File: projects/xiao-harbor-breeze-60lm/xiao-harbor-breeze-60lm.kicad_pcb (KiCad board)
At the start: 2 copper layers, 45.8 x 48.3 mm, 43 parts, among them CN1 XY122R-5.08-2P, CN2 XY122R-5.08-2P, J1 1165SDIG-07, J2 1165SDIG-07, Q1 UMW8205A, U1 BQ25185DLHR, U2 ME6210A33PG, U3 DW01A_C351410

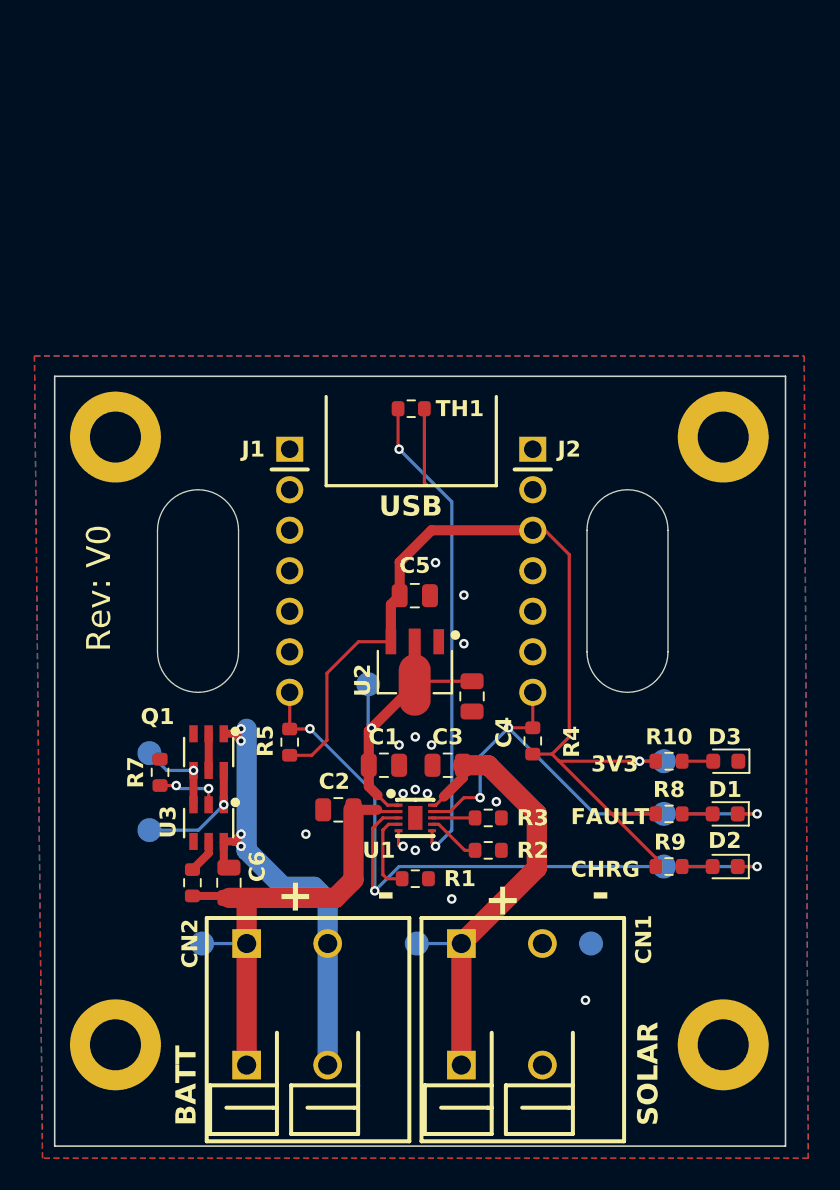
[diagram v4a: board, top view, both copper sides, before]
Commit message: Add user documented LED jumpers
Indicates to users that the LEDs are optional and documents how and
where to cut to conserve power.
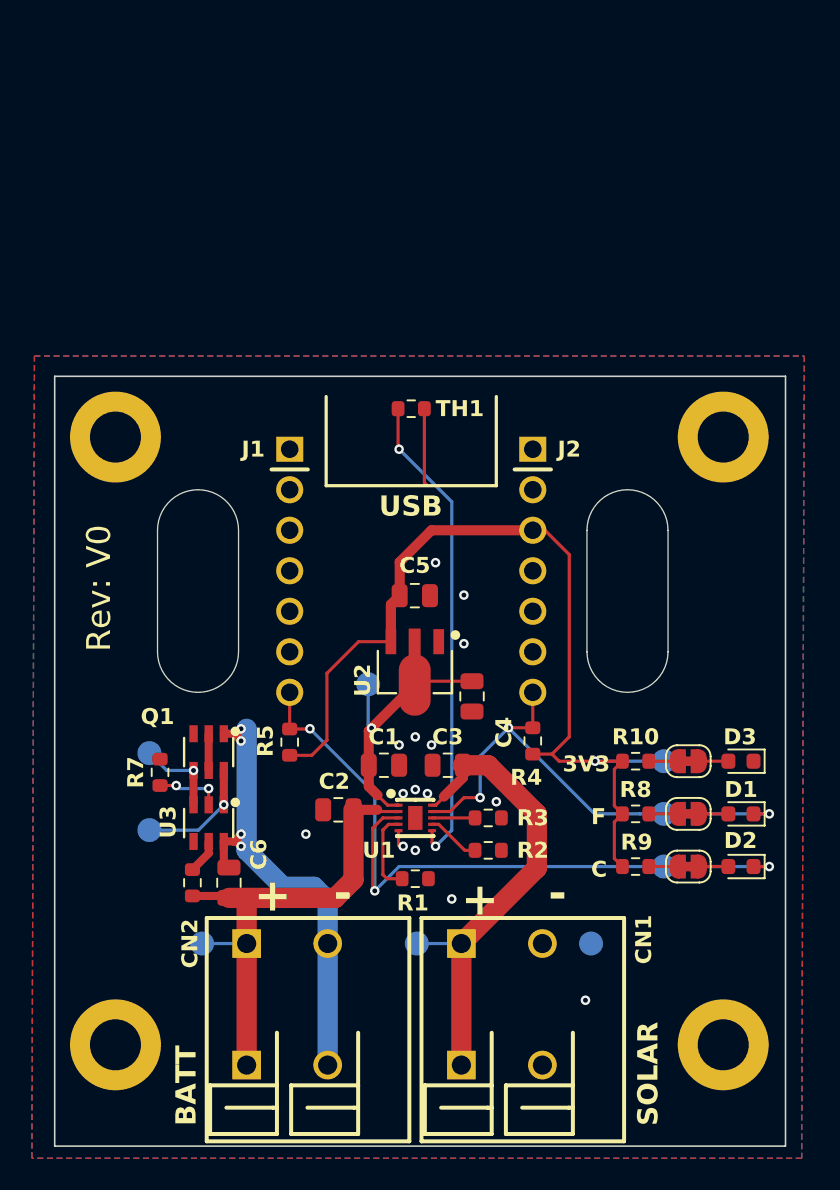
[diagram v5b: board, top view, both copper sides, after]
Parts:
- added JP1: SolderJumper_2_Bridged, Jumper:SolderJumper-2_P1.3mm_Bridged_RoundedPad1.0x1.5mm, F.Cu at (165.6, 100.6)
- added JP2: SolderJumper_2_Bridged, Jumper:SolderJumper-2_P1.3mm_Bridged_RoundedPad1.0x1.5mm, F.Cu at (165.6, 103.9)
- added JP3: SolderJumper_2_Bridged, Jumper:SolderJumper-2_P1.3mm_Bridged_RoundedPad1.0x1.5mm, F.Cu at (165.6, 97.3)
- moved R10 2.09 mm to (162.3, 97.3)
- moved R8 2.09 mm to (162.3, 100.6)
- moved R9 2.09 mm to (162.3, 103.9)
- moved D1 0.99 mm to (168.9, 100.6)
- moved D2 0.99 mm to (168.9, 103.9)
- moved D3 0.95 mm to (168.9, 97.3)
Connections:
- R10 pad 2: Net-(D3-A) -> Net-(JP3-B)
- R8 pad 2: Net-(D1-A) -> Net-(JP1-B)
- R9 pad 2: Net-(D2-A) -> Net-(JP2-B)
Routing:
- net +3V3: track 63.3 -> 59.6 mm
- net Net-(JP3-B): track 0.00 -> 1.83 mm
- net Net-(JP2-B): track 0.00 -> 1.83 mm
- net Net-(JP1-B): track 0.00 -> 1.83 mm
- net /STAT2: track 47.1 -> 47.6 mm
- net /STAT1: track 31.3 -> 31.8 mm
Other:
- board text added: "C"
- board text added: "F"
- board text removed: "CHRG"
- board text removed: "FAULT"

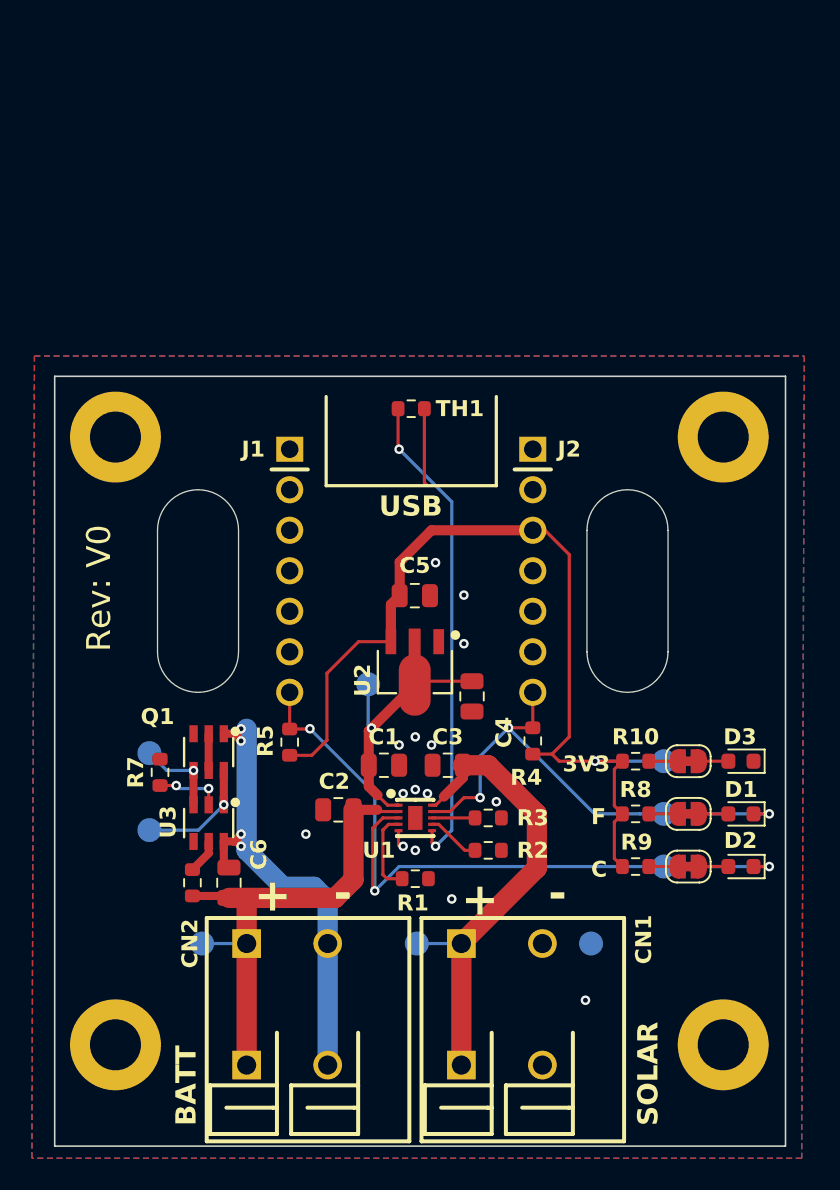
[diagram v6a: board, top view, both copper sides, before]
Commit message: Fix GLB output; Vendor all libraries
The kicad binaries for Ubuntu 24.04 are linked against a buggy version
of OCCT. The most direct solution here was simply to upgrade to Ubuntu 25.04.

Additionally all referenced libraries are now vendored under lib/. This
ensures that there are no conflicts between the container definition and
the host.

Due to this, the entire lib/ directory is now tracked in git lfs.
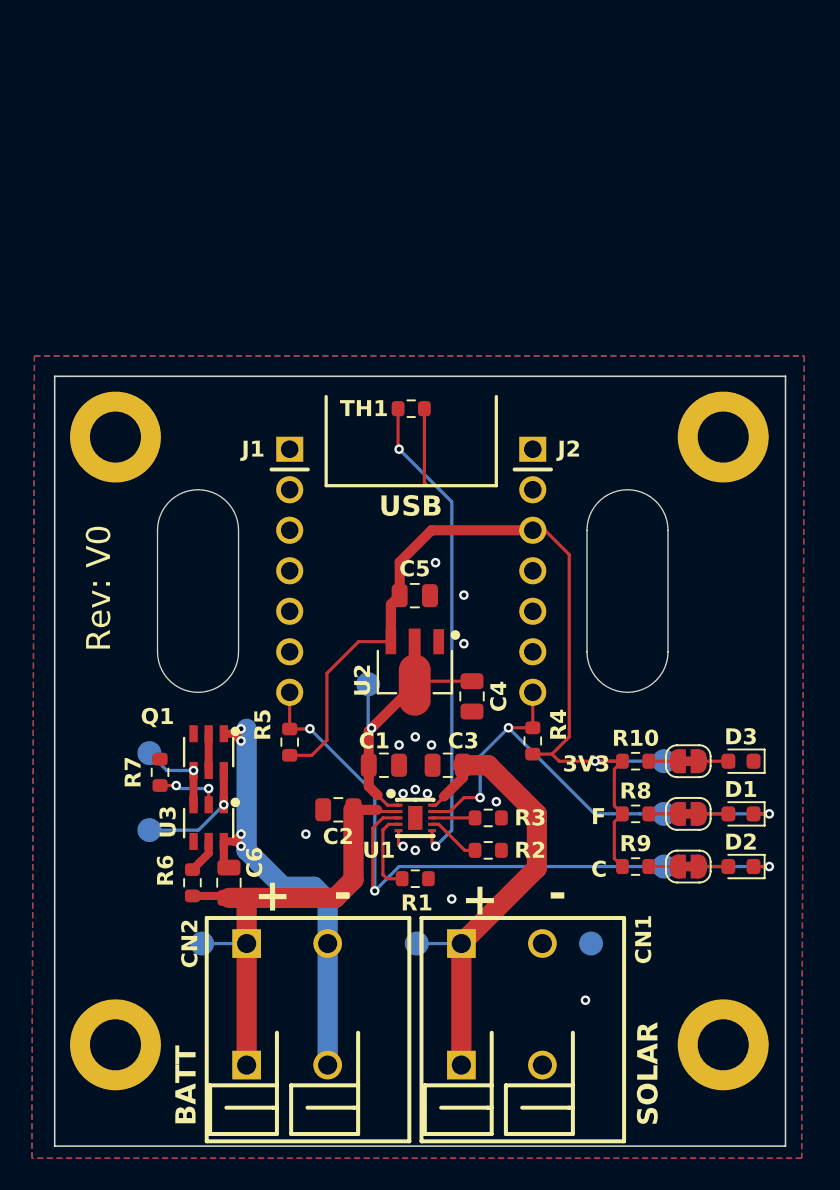
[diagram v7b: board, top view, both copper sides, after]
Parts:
- C1, C2, C3, C4, C5, C6: footprint Capacitor_SMD:C_0805_2012Metric -> Capacitor_SMD_Vendor:C_0805_2012Metric
- D1, D2, D3: footprint LED_SMD:LED_0603_1608Metric -> LED_SMD_Vendor:LED_0603_1608Metric
- H1, H2, H3, H4: footprint MountingHole:MountingHole_3.2mm_M3_ISO7380_Pad -> MountingHole_Vendor:MountingHole_3.2mm_M3_ISO7380_Pad
- JP1, JP2, JP3: footprint Jumper:SolderJumper-2_P1.3mm_Bridged_RoundedPad1.0x1.5mm -> Jumper_Vendor:SolderJumper-2_P1.3mm_Bridged_RoundedPad1.0x1.5mm
- R1, R10, R2, R3, R4, R5, R6, R7, R8, R9, TH1: footprint Resistor_SMD:R_0603_1608Metric -> Resistor_SMD_Vendor:R_0603_1608Metric
- TP1, TP2, TP3, TP4, TP5, TP6, TP7, TP8, TP9: footprint TestPoint:TestPoint_Pad_D1.5mm -> TestPoint_Vendor:TestPoint_Pad_D1.5mm

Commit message: Add zip-tie PCB documentation
Documents the purpose of the PCB cutout regions. Intended for users to
pass a zip-tie through and around to secure the XIAO development kit.
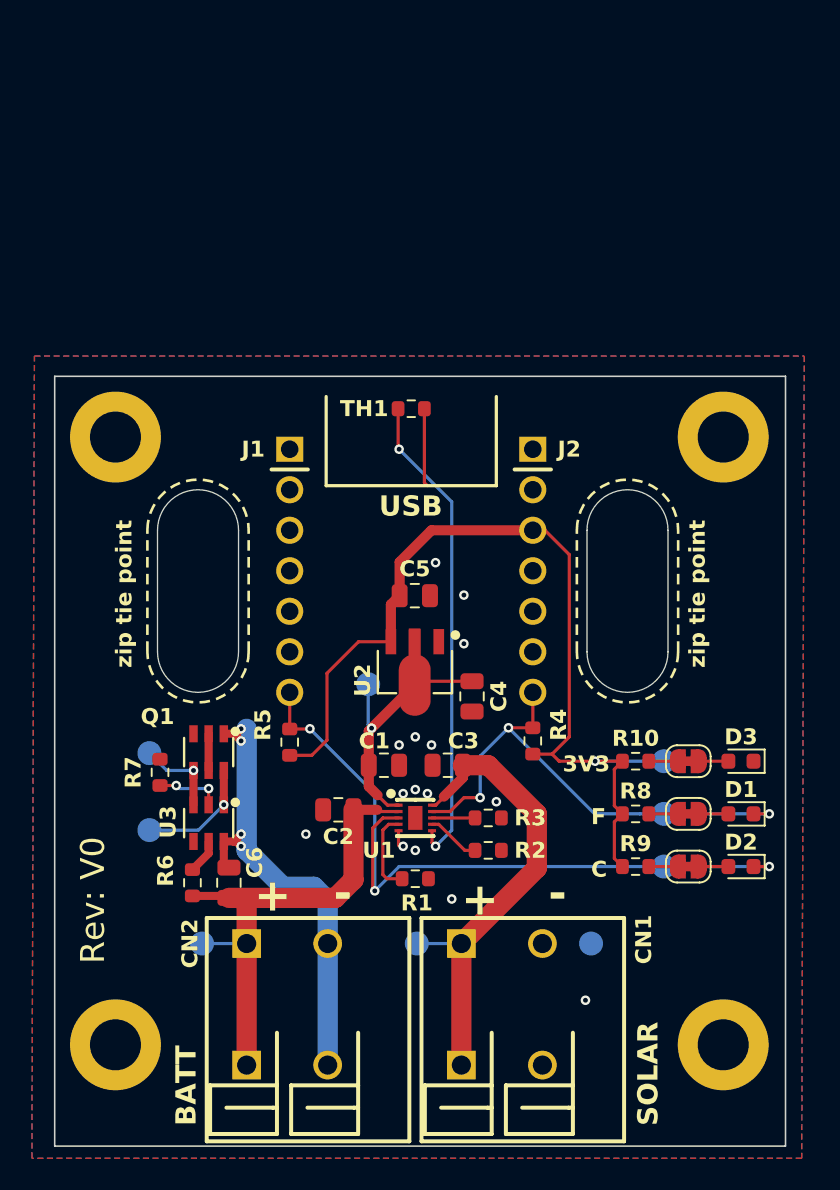
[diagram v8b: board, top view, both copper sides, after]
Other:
- board text added: "zip tie point"
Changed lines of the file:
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@@
+		(layer "F.SilkS")
+	)
+	(gr_arc
+		(start 164.973 90.424)
+		(mid 161.798 93.599)
+		(end 158.623 90.424)
+		(stroke
+			(width 0.1651)
+			(type dash_dot)
+		)
 		(layer "F.SilkS")
 	)
@@
 		)
 		(layer "F.SilkS")
+	)
+	(gr_arc
+		(start 138.049 90.424)
+		(mid 134.874 93.599)
+		(end 131.699 90.424)
+		(stroke
+			(width 0.1651)
+			(type dash_dot)
+		)
+		(layer "F.SilkS")
+	)
+	(gr_arc
+		(start 131.699 82.804)
+		(mid 134.874 79.629)
+		(end 138.049 82.804)
+		(stroke
+			(width 0.1651)
+			(type dash_dot)
+		)
+		(layer "F.SilkS")
+	)
+	(gr_line
+		(start 131.699 90.424)
+		(end 131.699 82.804)
+		(stroke
+			(width 0.1651)
+			(type dash_dot)
+		)
+		(layer "F.SilkS")
+	)
+	(gr_line
+		(start 164.973 90.424)
+		(end 164.973 82.804)
+		(stroke
+			(width 0.1651)
+			(type dash_dot)
+		)
+		(layer "F.SilkS")
+	)
+	(gr_line
+		(start 158.623 90.424)
+		(end 158.623 82.804)
+		(stroke
+			(width 0.1651)
+			(type dash_dot)
+		)
+		(layer "F.SilkS")
+	)
+	(gr_line
+		(start 138.049 90.424)
+		(end 138.049 82.804)
+		(stroke
+			(width 0.1651)
+			(type dash_dot)
+		)
+		(layer "F.SilkS")
+	)
+	(gr_arc
+		(start 158.623 82.804)
+		(mid 161.798 79.629)
+		(end 164.973 82.804)
+		(stroke
+			(width 0.1651)
+			(type dash_dot)
+		)
+		(layer "F.SilkS")
+	)
+	(gr_arc
+		(start 131.699 82.804)
+		(mid 134.874 79.629)
+		(end 138.049 82.804)
+		(stroke
+			(width 0.1651)
+			(type dash_dot)
+		)
+		(layer "B.SilkS")
+	)
+	(gr_arc
+		(start 158.623 82.804)
+		(mid 161.798 79.629)
+		(end 164.973 82.804)
+		(stroke
+			(width 0.1651)
+			(type dash_dot)
+		)
+		(layer "B.SilkS")
+	)
+	(gr_line
+		(start 164.973 90.424)
+		(end 164.973 82.804)
+		(stroke
+			(width 0.1651)
+			(type dash_dot)
+		)
+		(layer "B.SilkS")
+	)
+	(gr_arc
+		(start 138.049 90.424)
+		(mid 134.874 93.599)
+		(end 131.699 90.424)
+		(stroke
+			(width 0.1651)
+			(type dash_dot)
+		)
+		(layer "B.SilkS")
+	)
+	(gr_line
+		(start 131.699 90.424)
+		(end 131.699 82.804)
+		(stroke
+			(width 0.1651)
+			(type dash_dot)
+		)
+		(layer "B.SilkS")
+	)
+	(gr_line
+		(start 138.049 90.424)
+		(end 138.049 82.804)
+		(stroke
+			(width 0.1651)
+			(type dash_dot)
+		)
+		(layer "B.SilkS")
+	)
+	(gr_line
+		(start 158.623 90.424)
+		(end 158.623 82.804)
+		(stroke
+			(width 0.1651)
+			(type dash_dot)
+		)
+		(layer "B.SilkS")
+	)
+	(gr_arc
+		(start 164.973 90.424)
+		(mid 161.798 93.599)
+		(end 158.623 90.424)
+		(stroke
+			(width 0.1651)
+			(type dash_dot)
+		)
+		(layer "B.SilkS")
 	)
 	(gr_line
@@
 		)
 	)
+	(gr_text "zip tie point"
+		(at 166.763646 91.433676 90)
+		(layer "F.SilkS")
+		(effects
+			(font
+				(size 1 1)
+				(thickness 0.1651)
+				(bold yes)
+			)
+			(justify left bottom)
+		)
+	)
 	(gr_text "BATT"
 		(at 134.874 120.142 90)
@@
 		)
 	)
+	(gr_text "zip tie point"
+		(at 130.822646 91.433676 90)
+		(layer "F.SilkS")
+		(effects
+			(font
+				(size 1 1)
+				(thickness 0.1651)
+				(bold yes)
+			)
+			(justify left bottom)
+		)
+	)
 	(gr_text "F"
 		(at 159.512 101.346 0)
@@
 	)
 	(gr_text "Rev: V0"
-		(at 129.54 90.424 90)
+		(at 129.159 109.982 90)
 		(layer "F.SilkS")
 		(effects
@@
 		)
 	)
+	(gr_text "zip tie point"
+		(at 165.849354 91.433676 -90)
+		(layer "B.SilkS")
+		(effects
+			(font
+				(size 1 1)
+				(thickness 0.1651)
+				(bold yes)
+			)
+			(justify left bottom mirror)
+		)
+	)
 	(gr_text "flyovermesh.org"
 		(at 154.178 112.268 0)
 		(layer "B.SilkS")
 		(effects
+			(font
+				(size 1 1)
+				(thickness 0.1651)
+				(bold yes)
+			)
+			(justify left bottom mirror)
+		)
+	)
+	(gr_text "zip tie point"
+		(at 129.908354 91.433676 -90)
+		(layer "B.SilkS")
+		(effects
